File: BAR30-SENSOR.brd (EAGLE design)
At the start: 11.5 x 11.5 mm, 16 parts, among them Q1 BSS138, Q2 BSS138

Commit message: Change voltage regulator from zener to LDO.
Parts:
- removed R1: 1K, resistor:R0402
- removed U$2: 3.3V 100mW, BR-Eagle-Library:SOD523
- added C2: 2.2uF, resistor:C0402
- added U$8: VREG-MIC5365, BlueRobotics-Main:SC70-5L
- C1: value 0.47uF -> 2.2uF
- U$7: value LOGOBR-LOGO-M -> LOGOBR-LOGO-S; device BR-Eagle-Library:BR-LOGO-MEDIUM -> BR-Eagle-Library:BR-LOGO-SMALL
- moved U$7 6.08 mm to (8.30, 5.73), flipped to the bottom
- moved C1 4.01 mm to (10.8, 6.04), turned to 180 degrees
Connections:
- net 3.3V: now also U$8.1; no longer R1.2, U$2.C
- net GND: now also C2.2, U$8.2; no longer U$2.A
- net VCC: now also C2.1, U$8.3, U$8.4; no longer R1.1
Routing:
- net GND: track 8.66 -> 5.28 mm, vias 2 -> 3
- net VCC: track 6.72 -> 10.1 mm
- net 3.3V: track 19.3 -> 17.8 mm
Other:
- board text added: "rev2"
- board text removed: "rev1"

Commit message: Fixed incorrect regulator footprint.
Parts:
- C1, C2: value 2.2uF -> 1uF
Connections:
- net 3.3V: now also U$8.5; no longer U$8.1
- net VCC: now also U$8.1; no longer U$8.4
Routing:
- net 3.3V: track 17.8 -> 15.4 mm
- net VCC: track 10.1 -> 12.4 mm
- net GND: vias 3 -> 4
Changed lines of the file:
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@@
 </autorouter>
 <elements>
-<element name="C1" library="resistor" package="C0402" value="2.2uF" x="10.82005" y="6.037228125" smashed="yes" rot="R180"/>
+<element name="C1" library="resistor" package="C0402" value="1uF" x="10.82005" y="6.037228125" smashed="yes" rot="R180"/>
 <element name="Q1" library="SparkFun-DiscreteSemi" package="SOT323" value="BSS138" x="3.457015625" y="6.36045" smashed="yes">
 <attribute name="PROD_ID" value="TRANS-11151" x="3.457015625" y="6.36045" size="1.778" layer="27" display="off"/>
@@
 <element name="U$7" library="BR-Eagle-Library" package="BR-LOGO-SMALL" value="LOGOBR-LOGO-S" x="8.296571875" y="5.731128125" rot="MR0"/>
 <element name="U$8" library="BlueRobotics-Main" package="SC70-5L" value="VREG-MIC5365" x="10.85054375" y="8.583109375" smashed="yes" rot="R180"/>
-<element name="C2" library="resistor" package="C0402" value="2.2uF" x="8.495978125" y="10.65720625" smashed="yes" rot="R90"/>
+<element name="C2" library="resistor" package="C0402" value="1uF" x="8.495978125" y="10.65720625" smashed="yes" rot="R90"/>
 </elements>
 <signals>
@@
 <vertex x="0" y="0"/>
 </polygon>
-<via x="10.3228125" y="11.02294375" extent="1-16" drill="0.3556"/>
+<via x="10.824746875" y="10.596034375" extent="1-16" drill="0.3556"/>
+<via x="9.766515625" y="11.887265625" extent="1-16" drill="0.3556"/>
 </signal>
 <signal name="SCL_LV">
@@
 <wire x1="5.280009375" y1="3.010221875" x2="6.295403125" y2="4.025615625" width="0.254" layer="1"/>
 <contactref element="U$1" pad="2"/>
-<contactref element="U$8" pad="1"/>
+<contactref element="U$8" pad="5"/>
 <wire x1="7.492015625" y1="5.52045" x2="8.107015625" y2="6.13545" width="0.254" layer="1"/>
 <wire x1="11.47005" y1="6.037228125" x2="11.47005" y2="5.43839375" width="0.254" layer="1"/>
@@
 <wire x1="11.200509375" y1="5.168853125" x2="9.0736125" y2="5.168853125" width="0.254" layer="1"/>
 <wire x1="9.0736125" y1="5.168853125" x2="8.107015625" y2="6.13545" width="0.254" layer="1"/>
-<wire x1="11.47005" y1="6.037228125" x2="11.47005" y2="6.330628125" width="0.254" layer="1"/>
-<wire x1="11.47005" y1="6.330628125" x2="12.07014375" y2="6.930721875" width="0.254" layer="1"/>
-<wire x1="12.07014375" y1="6.930721875" x2="12.07014375" y2="8.963509375" width="0.254" layer="1"/>
-<wire x1="12.07014375" y1="8.963509375" x2="11.50054375" y2="9.533109375" width="0.254" layer="1"/>
+<wire x1="11.47005" y1="6.037228125" x2="11.47005" y2="7.602615625" width="0.254" layer="1"/>
+<wire x1="11.47005" y1="7.602615625" x2="11.50054375" y2="7.633109375" width="0.254" layer="1"/>
 </signal>
 <signal name="VCC">
@@
 <wire x1="7.087015625" y1="10.01545" x2="7.067015625" y2="10.01545" width="0.254" layer="1"/>
 <wire x1="7.067015625" y1="10.01545" x2="5.787015625" y2="11.29545" width="0.254" layer="1"/>
-<contactref element="U$8" pad="4"/>
+<contactref element="U$8" pad="1"/>
 <contactref element="U$8" pad="3"/>
 <contactref element="C2" pad="1"/>
@@
 <wire x1="8.487734375" y1="10.01545" x2="8.495978125" y2="10.00720625" width="0.254" layer="1"/>
 <wire x1="8.495978125" y1="10.00720625" x2="9.726446875" y2="10.00720625" width="0.254" layer="1"/>
-<wire x1="9.726446875" y1="10.00720625" x2="10.20054375" y2="9.533109375" width="0.254" layer="1"/>
-<wire x1="10.20054375" y1="9.533109375" x2="10.20054375" y2="7.633109375" width="0.254" layer="1"/>
+<wire x1="11.50629375" y1="9.527359375" x2="11.50054375" y2="9.533109375" width="0.254" layer="1"/>
+<wire x1="10.20054375" y1="9.533109375" x2="9.726446875" y2="10.00720625" width="0.254" layer="1"/>
+<wire x1="11.50054375" y1="9.533109375" x2="11.50054375" y2="10.9094875" width="0.254" layer="1"/>
+<wire x1="11.50054375" y1="10.9094875" x2="11.1764375" y2="11.23359375" width="0.254" layer="1"/>
+<wire x1="11.1764375" y1="11.23359375" x2="10.331909375" y2="11.23359375" width="0.254" layer="1"/>
+<wire x1="10.331909375" y1="11.23359375" x2="9.695728125" y2="10.5974125" width="0.254" layer="1"/>
+<wire x1="9.695728125" y1="10.5974125" x2="9.695728125" y2="10.037925" width="0.254" layer="1"/>
+<wire x1="9.695728125" y1="10.037925" x2="9.726446875" y2="10.00720625" width="0.254" layer="1"/>
 </signal>
 <signal name="SCL_HV">

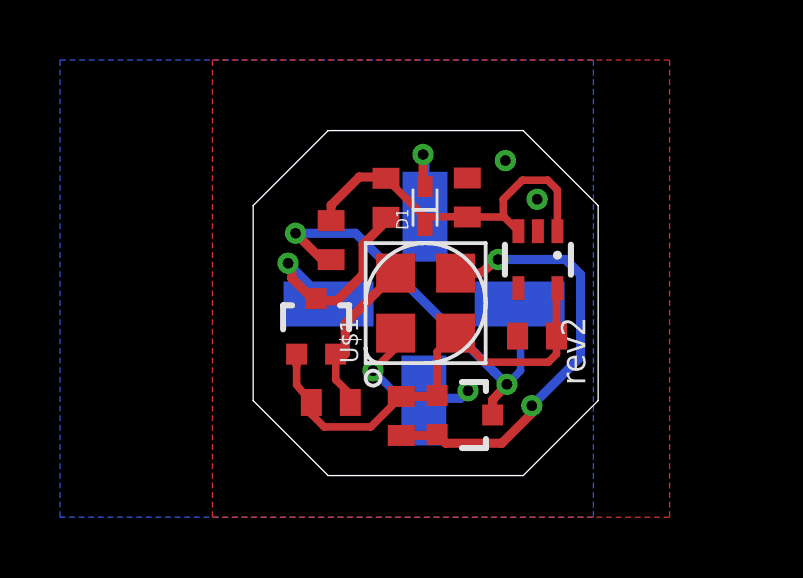
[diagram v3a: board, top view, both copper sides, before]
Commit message: Added a ground via and change silk screen on bottom to reflect proper voltage range.
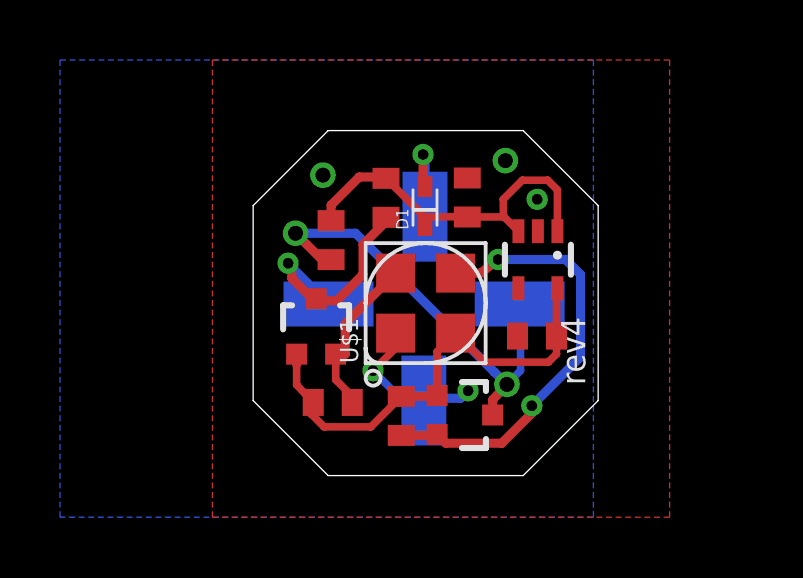
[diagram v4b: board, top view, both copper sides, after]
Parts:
- moved R2 0.06 mm to (4.01, 3.82)
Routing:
- net GND: vias 4 -> 5
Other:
- board text added: "+2.5-5.5V"
- board text added: "rev4"
- board text removed: "+2-6V"
- board text removed: "rev2"
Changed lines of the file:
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@@
 <layer number="27" name="tValues" color="7" fill="1" visible="yes" active="yes"/>
 <layer number="28" name="bValues" color="7" fill="1" visible="yes" active="yes"/>
-<layer number="29" name="tStop" color="7" fill="3" visible="no" active="yes"/>
-<layer number="30" name="bStop" color="7" fill="6" visible="no" active="yes"/>
+<layer number="29" name="tStop" color="7" fill="3" visible="yes" active="yes"/>
+<layer number="30" name="bStop" color="7" fill="6" visible="yes" active="yes"/>
 <layer number="31" name="tCream" color="7" fill="4" visible="no" active="yes"/>
 <layer number="32" name="bCream" color="7" fill="5" visible="no" active="yes"/>
@@
 <wire x1="12.858390625" y1="3.88715" x2="10.358390625" y2="1.38715" width="0.025" layer="20"/>
 <wire x1="3.858390625" y1="1.38715" x2="10.358390625" y2="1.38715" width="0.025" layer="20"/>
-<text x="12.43070625" y="4.408709375" size="0.8128" layer="21" font="vector" ratio="12" rot="R90">rev2</text>
+<text x="12.43070625" y="4.408709375" size="0.8128" layer="21" font="vector" ratio="12" rot="R90">rev4</text>
 <text x="3.497846875" y="3.6989375" size="0.6096" layer="22" font="vector" ratio="12" rot="MR225" align="center">Blue
 Robotics</text>
@@
 <text x="4.233146875" y="8.517353125" size="1.016" layer="22" font="vector" ratio="12" rot="MR0" align="center">SDA</text>
 <text x="3.748434375" y="5.705171875" size="0.8128" layer="22" font="vector" ratio="12" rot="MR0" align="center">WHITE</text>
-<text x="8.5632375" y="10.262840625" size="1.016" layer="22" font="vector" ratio="12" rot="MR270" align="center">+2-6V</text>
+<text x="8.5632375" y="10.262840625" size="0.6096" layer="22" font="vector" ratio="12" rot="MR270" align="center">+2.5-5.5V</text>
 <text x="5.7034375" y="10.780025" size="0.8128" layer="22" font="vector" ratio="12" rot="MR270" align="center">RED</text>
 <text x="8.3370375" y="2.79601875" size="0.8128" layer="22" font="vector" ratio="12" rot="MR270" align="center">GND</text>
@@
 </class>
 </classes>
-<designrules name="OSHPark">
+<designrules name="OSHPark *">
 <description language="de">&lt;b&gt;EAGLE Design Rules&lt;/b&gt;
 &lt;p&gt;
@@
 <param name="mlMinCreamFrame" value="0mil"/>
 <param name="mlMaxCreamFrame" value="0mil"/>
-<param name="mlViaStopLimit" value="0mil"/>
+<param name="mlViaStopLimit" value="30mil"/>
 <param name="srRoundness" value="0"/>
 <param name="srMinRoundness" value="0mil"/>
@@
 <attribute name="PROD_ID" value="TRANS-11151" x="8.417015625" y="3.40545" size="1.778" layer="27" rot="R270" display="off"/>
 </element>
-<element name="R2" library="resistor" package="R0402" value="10K" x="3.947365625" y="3.8245125" smashed="yes" rot="R180"/>
+<element name="R2" library="resistor" package="R0402" value="10K" x="4.011309375" y="3.8245125" smashed="yes" rot="R180"/>
 <element name="R3" library="resistor" package="R0402" value="10K" x="5.787015625" y="10.64545" smashed="yes" rot="R90"/>
 <element name="R4" library="resistor" package="R0402" value="10K" x="6.295403125" y="3.375615625" smashed="yes" rot="R90"/>
@@
 </polygon>
 <via x="10.824746875" y="10.596034375" extent="1-16" drill="0.3556"/>
-<via x="9.766515625" y="11.887265625" extent="1-16" drill="0.3556"/>
+<via x="9.766515625" y="11.887265625" extent="1-16" drill="0.5"/>
+<via x="3.684715625" y="11.400146875" extent="1-16" drill="0.5"/>
 </signal>
 <signal name="SCL_LV">
@@
 <wire x1="4.427015625" y1="5.43545" x2="4.427015625" y2="6.45545" width="0.3048" layer="1"/>
 <wire x1="4.427015625" y1="6.45545" x2="6.107015625" y2="8.13545" width="0.3048" layer="1"/>
-<wire x1="4.597365625" y1="3.8245125" x2="4.591975" y2="4.099628125" width="0.254" layer="1"/>
+<wire x1="4.661309375" y1="3.8245125" x2="4.591975" y2="4.099628125" width="0.254" layer="1"/>
 <wire x1="4.591975" y1="4.099628125" x2="4.11169375" y2="4.579909375" width="0.254" layer="1"/>
 <wire x1="4.11169375" y1="4.579909375" x2="4.11169375" y2="5.430771875" width="0.254" layer="1"/>
@@
 <wire x1="7.492015625" y1="4.05545" x2="7.492015625" y2="5.52045" width="0.254" layer="1"/>
 <wire x1="2.807015625" y1="5.089" x2="2.807015625" y2="4.411878125" width="0.254" layer="1"/>
-<wire x1="2.807015625" y1="4.411878125" x2="3.297365625" y2="3.8245125" width="0.254" layer="1"/>
-<wire x1="3.297365625" y1="3.8245125" x2="3.291975" y2="3.44260625" width="0.254" layer="1"/>
+<wire x1="2.807015625" y1="4.411878125" x2="3.361309375" y2="3.8245125" width="0.254" layer="1"/>
+<wire x1="3.361309375" y1="3.8245125" x2="3.291975" y2="3.44260625" width="0.254" layer="1"/>
 <wire x1="3.291975" y1="3.44260625" x2="3.724359375" y2="3.010221875" width="0.254" layer="1"/>
 <wire x1="3.724359375" y1="3.010221875" x2="5.280009375" y2="3.010221875" width="0.254" layer="1"/>
@@
 <wire x1="9.342015625" y1="3.40545" x2="9.342015625" y2="3.91045" width="0.3048" layer="1"/>
 <wire x1="9.342015625" y1="3.91045" x2="9.817825" y2="4.429" width="0.3048" layer="1"/>
-<via x="9.817825" y="4.429" extent="1-16" drill="0.3556"/>
+<via x="9.817825" y="4.429" extent="1-16" drill="0.5"/>
 <wire x1="10.272015625" y1="7.07545" x2="10.242015625" y2="7.10545" width="0.3048" layer="16"/>
 <wire x1="3.957015625" y1="8.58545" x2="3.652015625" y2="8.58545" width="0.3048" layer="1"/>
 <wire x1="3.652015625" y1="8.58545" x2="2.772015625" y2="9.46545" width="0.3048" layer="1"/>
-<via x="2.772015625" y="9.46545" extent="1-16" drill="0.3556"/>
+<via x="2.772015625" y="9.46545" extent="1-16" drill="0.5"/>
 <wire x1="2.772015625" y1="9.46545" x2="4.772015625" y2="9.46545" width="0.3048" layer="16"/>
 <wire x1="4.772015625" y1="9.46545" x2="9.397015625" y2="4.84045" width="0.3048" layer="16"/>
